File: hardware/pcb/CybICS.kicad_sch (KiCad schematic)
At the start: 83 parts, among them J1 Raspberry_Pi_2_3, J2 Conn_01x03_Pin, J3 Conn_01x05_Pin, SW1 SW_Push, SW2 SW_Push, SW3 7*7*5-6P-L WX, U1 STM32G070RBTx

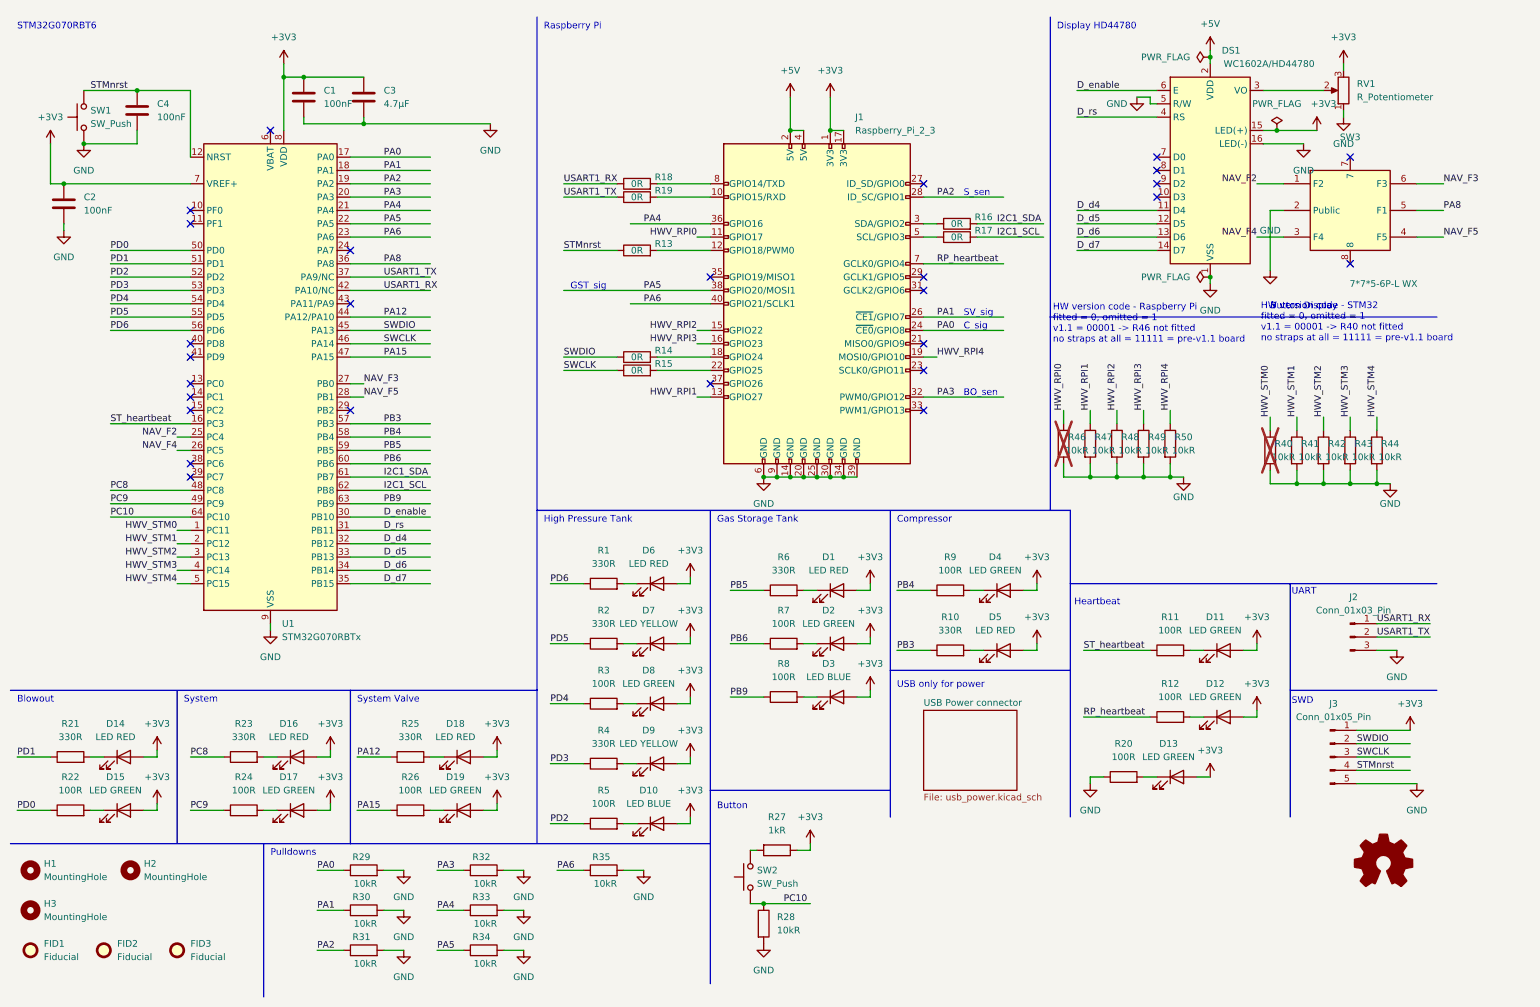
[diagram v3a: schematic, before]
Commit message: refactor(hardware): move the navigation directions to PC6, PC7, PD8, PD9
The four direction contacts move off PC4/PC5/PB0/PB1 (pins 25-28) onto
pins 38-41, at the maintainer's request:

  NAV_F2  U1.38  PC6
  NAV_F3  U1.39  PC7
  NAV_F4  U1.40  PD8
  NAV_F5  U1.41  PD9

The centre press stays on PA8, so firmware keeps its existing name for
the display button. Pins 38-41 are contiguous on the east edge of the
LQFP-64 at x=100.47, which should make the fan-out shorter than the
south-edge group would have.

PC4, PC5, PB0 and PB1 go back to unconnected with their no_connect flags
restored, so they are free again for a later change.

Verified with kicad-cli 10.0.6: ERC reports 0 violations, and the four
nets each carry exactly two nodes -- the switch contact and its MCU pin.
Measured against the state before the switch swap, the only nets that
differ are still +3V3 (lost R37.1), /PA8 (gained SW3.5, lost R36.1 and
the old SW3.1) and GND (gained SW3.2, lost R36.2); nothing else moved.
The schematic was rendered and the stubs sit clear of the surrounding
arrangement.

Co-Authored-By: Claude Opus 5 (1M context) <noreply@anthropic.com>
Claude-Session: https://claude.ai/code/session_011zbigHZaGiZii3etPu8DwT
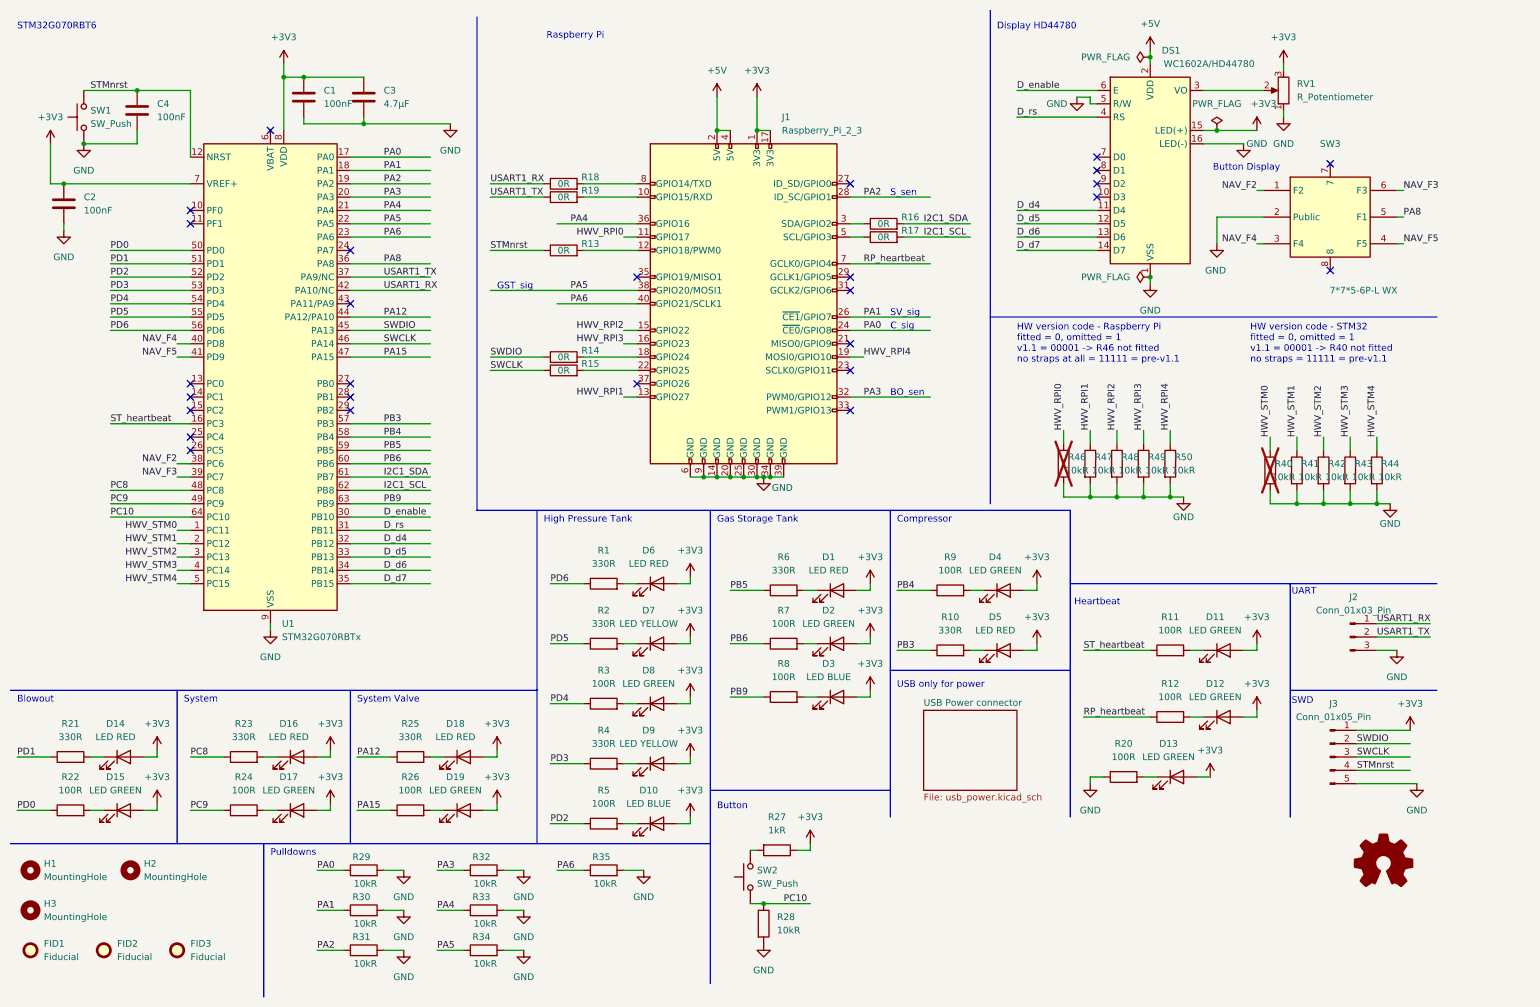
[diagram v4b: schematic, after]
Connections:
- net NAV_F2: now also U1.38 (PC6); no longer U1.25 (PC4)
- net NAV_F3: now also U1.39 (PC7); no longer U1.27 (PB0)
- net NAV_F4: now also U1.40 (PD8); no longer U1.26 (PC5)
- net NAV_F5: now also U1.41 (PD9); no longer U1.28 (PB1)
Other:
- note added: "HW version code - Raspberry Pi fitted = 0, omitted = 1 v1.1 = 00001 -> R46 not fitted no straps at all = 11111 = pre-v1.1"
- note added: "HW version code - STM32 fitted = 0, omitted = 1 v1.1 = 00001 -> R40 not fitted no straps = 11111 = pre-v1.1"
- note removed: "HW version code - Raspberry Pi fitted = 0, omitted = 1 v1.1 = 00001 -> R46 not fitted no straps at all = 11111 = pre-v1.1 board"
- note removed: "HW version code - STM32 fitted = 0, omitted = 1 v1.1 = 00001 -> R40 not fitted no straps at all = 11111 = pre-v1.1 board"
- moved on the sheet: DS1, J1, R13, R14, R15, R16, R17, R18, R19, R40, R41, R42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

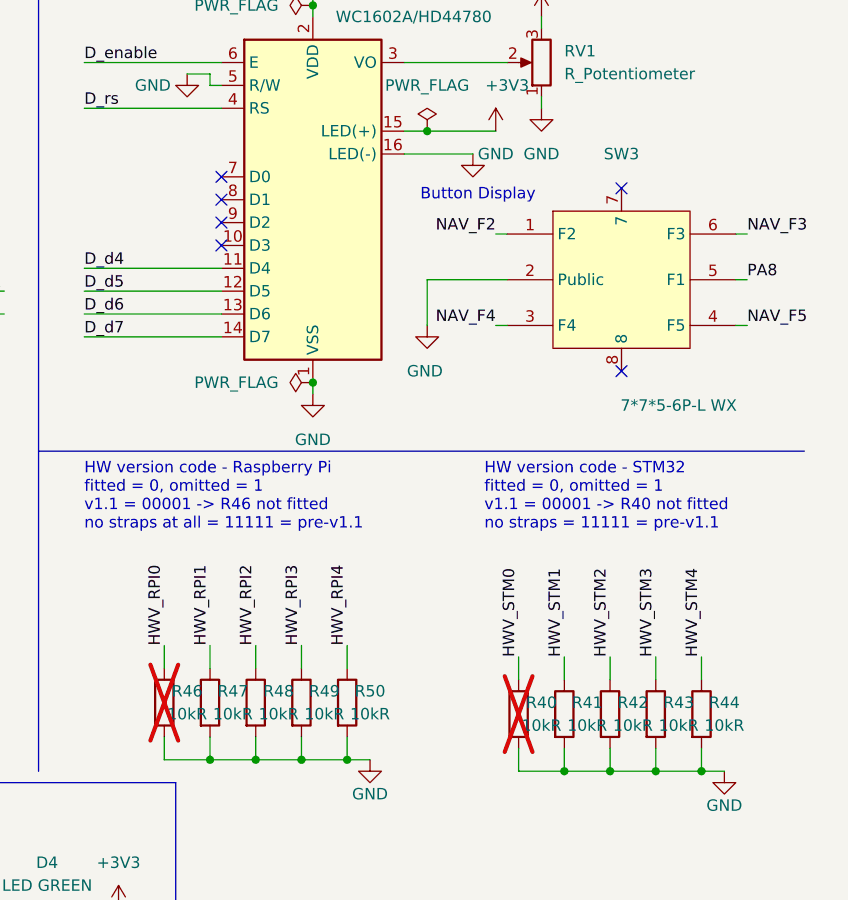
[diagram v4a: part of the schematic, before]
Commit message: fix(hardware): size the strap resistors and give the switch series limits
Two changes that both come down to reading a pin low reliably against the
STM32G0's weak pull-up, which the datasheet puts at 25k minimum, 40k
typical, 60k maximum.

The version straps were 10k. That is a divider against the internal
pull-up, and at the 25k end it sits at 0.94 V -- roughly 50 mV under a
V_IL of 0.3*VDD. Designed to the typical value it looks fine at 0.66 V,
but worst-case silicon could read a fitted strap as high. At 1k the same
worst case is 0.127 V, a margin of 0.86 V instead of 0.05 V. Current
through a fitted strap is 53-127 uA, which is nothing. C17513 is already
a basic part in this BOM, so the ten straps just move from the 10kR row
to the 1kR row and cost no new line and no feeder fee. R40 and R46 keep
their DNP flags, verified in both the schematic and the board.

The navigation switch gets a 1k in series with each of its five contacts
(R51-R55). This is not about levels -- a switch is a short or an open,
so the internal pull-up alone reads it correctly. It restores something
the old button had and this redesign had quietly dropped: R37 used to sit
in series, limiting the current if a pin were ever configured as an
output driving high while the button is pressed. Without it that is a
direct short to GND; with 1k it is 3.3 mA. 1k also keeps the closed-
contact level at 0.127 V worst case.

The common's GND leg was rerouted to x=248.92 so it clears the two
west-side resistors.

Verified with kicad-cli 10.0.6: ERC reports 0 violations and the netlist
shows each contact running SW3 -> 1k -> MCU pin, with SW3.2 on GND and
pins 7/8 unconnected. The switch area was rendered and checked.

Still to do on the board: Update PCB from Schematic, then place and route
R51-R55 -- they exist in the schematic only. The reference and value text
of the three east-side resistors still overlaps at the 5.08 mm pitch and
wants a nudge in eeschema.

Co-Authored-By: Claude Opus 5 (1M context) <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
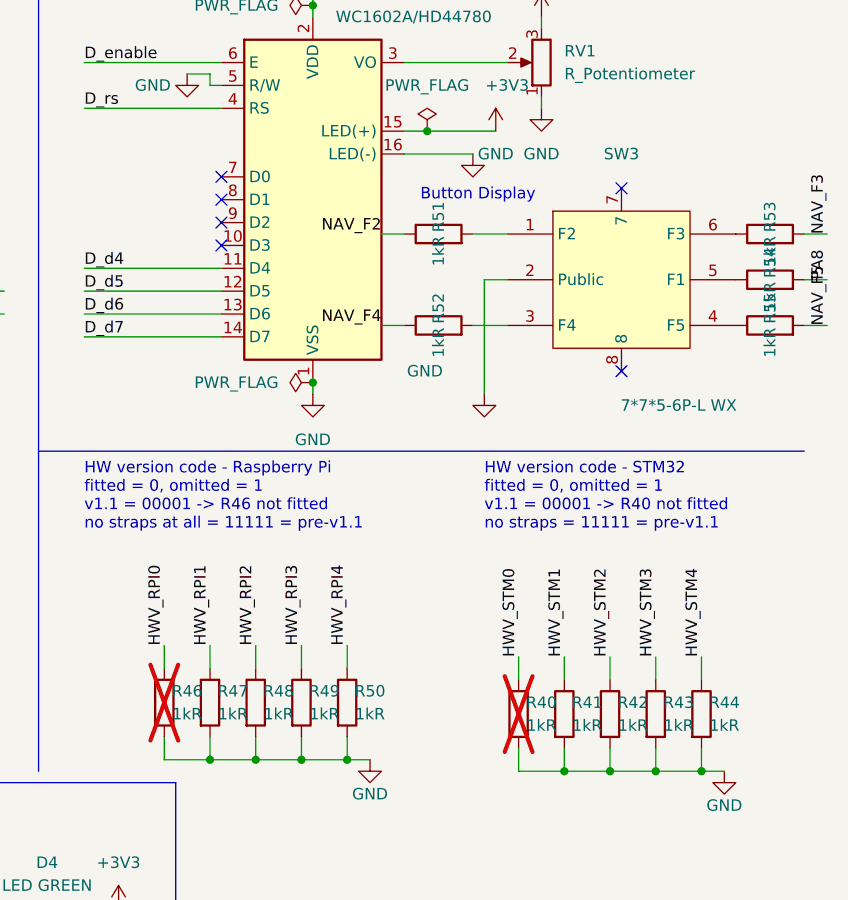
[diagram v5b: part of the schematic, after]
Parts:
- added R51, R52, R53, R54, R55: 1kR, Resistor_SMD:R_0805_2012Metric_Pad1.20x1.40mm_HandSolder, symbol Device:R
- R40, R41, R42, R43, R44, R46, R47, R48, R49, R50: value 10kR -> 1kR; JLCPCB Part # C17414 -> C17513
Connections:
- net NAV_F2: now also R51.1; no longer SW3.1 (F2)
- net NAV_F3: now also R53.2; no longer SW3.6 (F3)
- net NAV_F4: now also R52.1; no longer SW3.3 (F4)
- net NAV_F5: now also R55.2; no longer SW3.4 (F5)
- net PA8: now also R54.2; no longer SW3.5 (F1)
- new net: R55.1, SW3.4 (F5)
- new net: R53.1, SW3.6 (F3)
- new net: R52.2, SW3.3 (F4)
- new net: R51.2, SW3.1 (F2)
- new net: R54.1, SW3.5 (F1)
